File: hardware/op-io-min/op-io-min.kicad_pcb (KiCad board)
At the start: 2 copper layers, 19 x 85.7 mm, 18 parts, among them J1 USB_A, J2 RUN, J3 MIDI_IN, J4 MIDI_OUT, J5 USB_HEADER, U1 Teensy4.1, U2 6N138

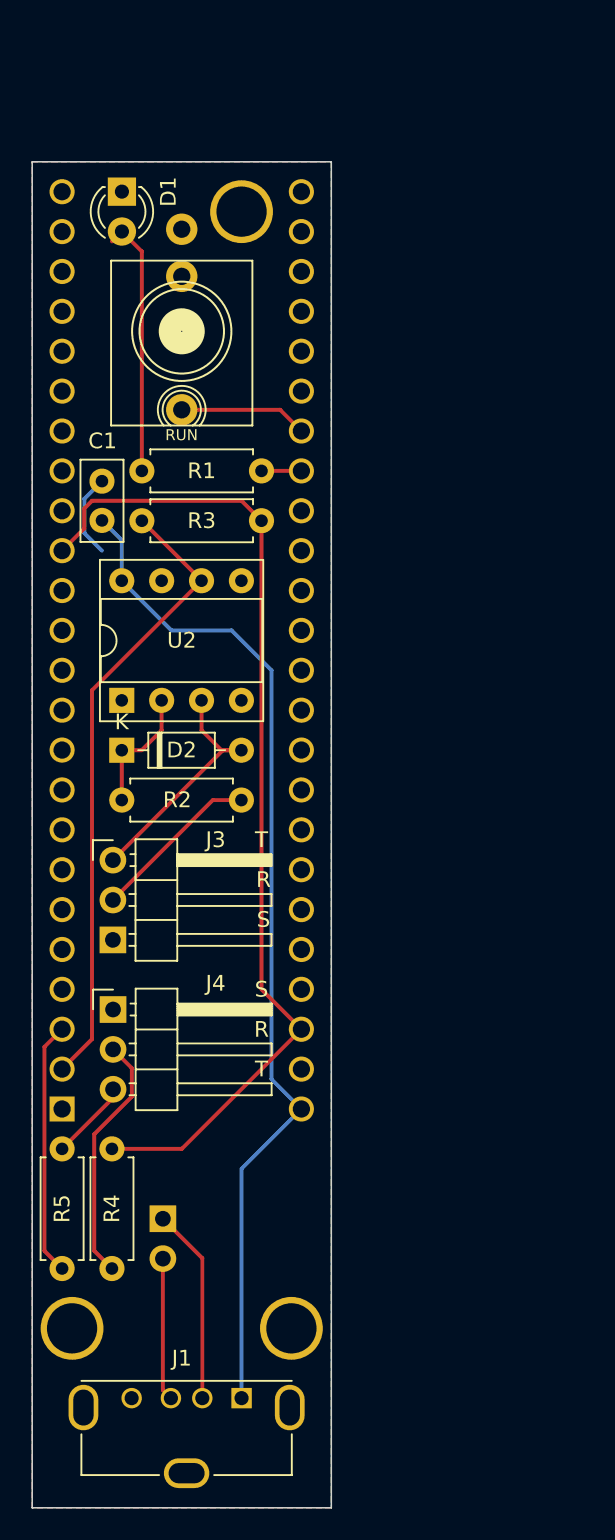
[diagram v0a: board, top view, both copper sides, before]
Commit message: added output impedance resistor
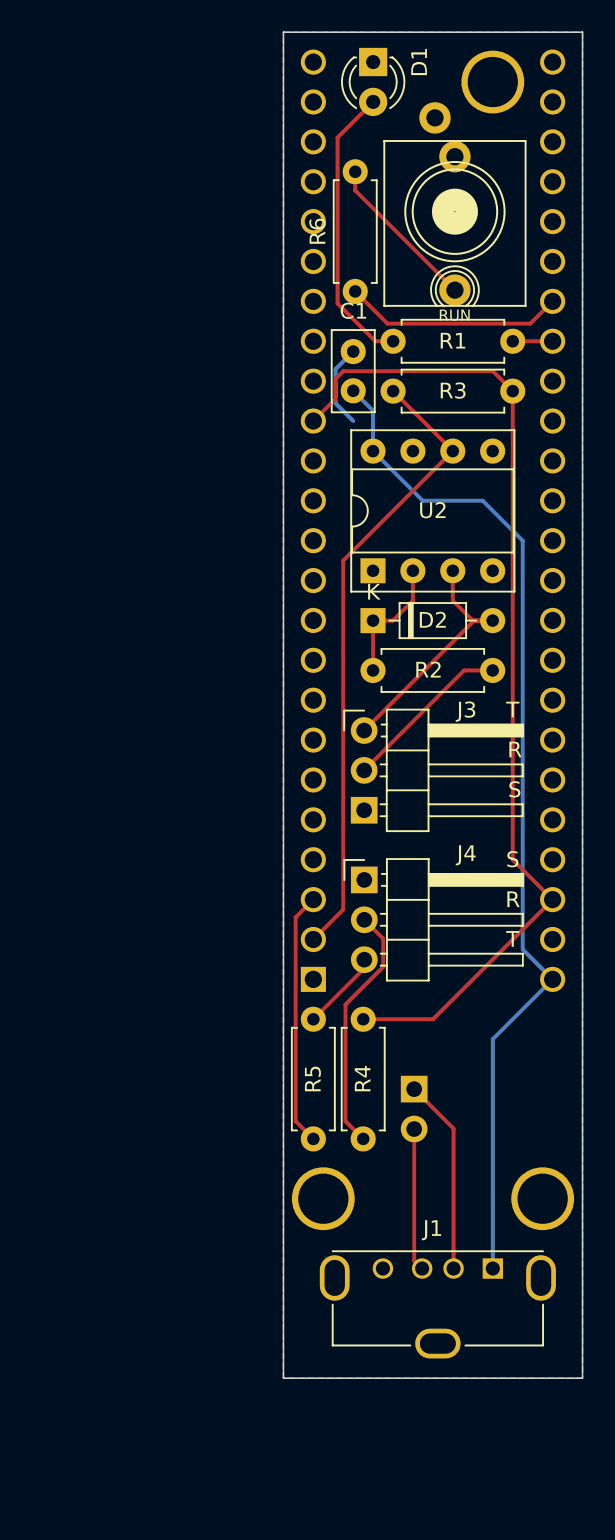
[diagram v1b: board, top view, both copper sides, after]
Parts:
- added R6: 1K, Resistor_THT:R_Axial_DIN0207_L6.3mm_D2.5mm_P7.62mm_Horizontal, F.Cu at (24.9, 33.7)
- moved J2 19.0 mm to (31.2, 28.6)
- moved R4 18.0 mm to (25.4, 87.6)
- moved C1 18.0 mm to (24.8, 40.0)
- moved D1 18.0 mm to (26.0, 19.0)
- moved D2 18.0 mm to (26.0, 54.6)
- moved H1 18.0 mm to (33.7, 20.3)
- moved J1 18.0 mm to (33.7, 95.9)
- moved J3 18.0 mm to (25.5, 61.6)
- moved R1 18.0 mm to (34.9, 36.8)
- moved R2 18.0 mm to (33.6, 57.8)
- moved R5 18.0 mm to (22.2, 80.0)
- moved U1 18.0 mm to (29.8, 48.3)
- moved U2 18.0 mm to (26.0, 51.4)
- moved H1 18.0 mm to (36.8, 91.4)
- moved H1 18.0 mm to (22.9, 91.4)
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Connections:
- J2 pad T: RUN -> Net-(J2-Tip)
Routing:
- net Net-(J2-Tip): track 0.00 -> 10.2 mm
- net RUN: track 8.18 -> 14.0 mm
- net Net-(D1-A): track 16.7 -> 18.3 mm
